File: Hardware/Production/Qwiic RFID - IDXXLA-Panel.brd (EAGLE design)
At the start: 25.4 x 30.5 mm, 60 parts, among them J2 SMD, J3 PTH, J4 SMD, J8 AVR_SPI_PROG_3X2TESTPOINTS, Q1 600mA/40V, U1 ATTINY84-ARDUINO, U2 ID-12/20SMD

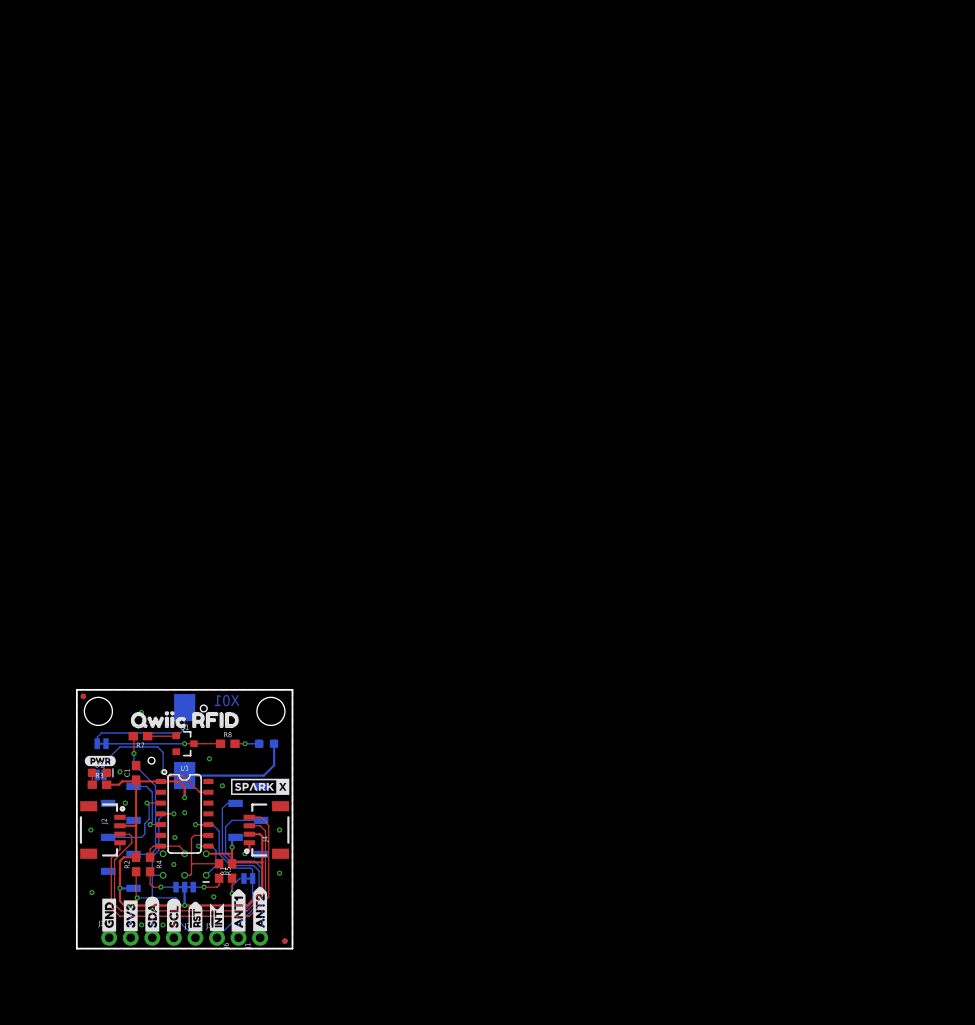
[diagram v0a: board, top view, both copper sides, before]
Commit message: Production Panel 3x3
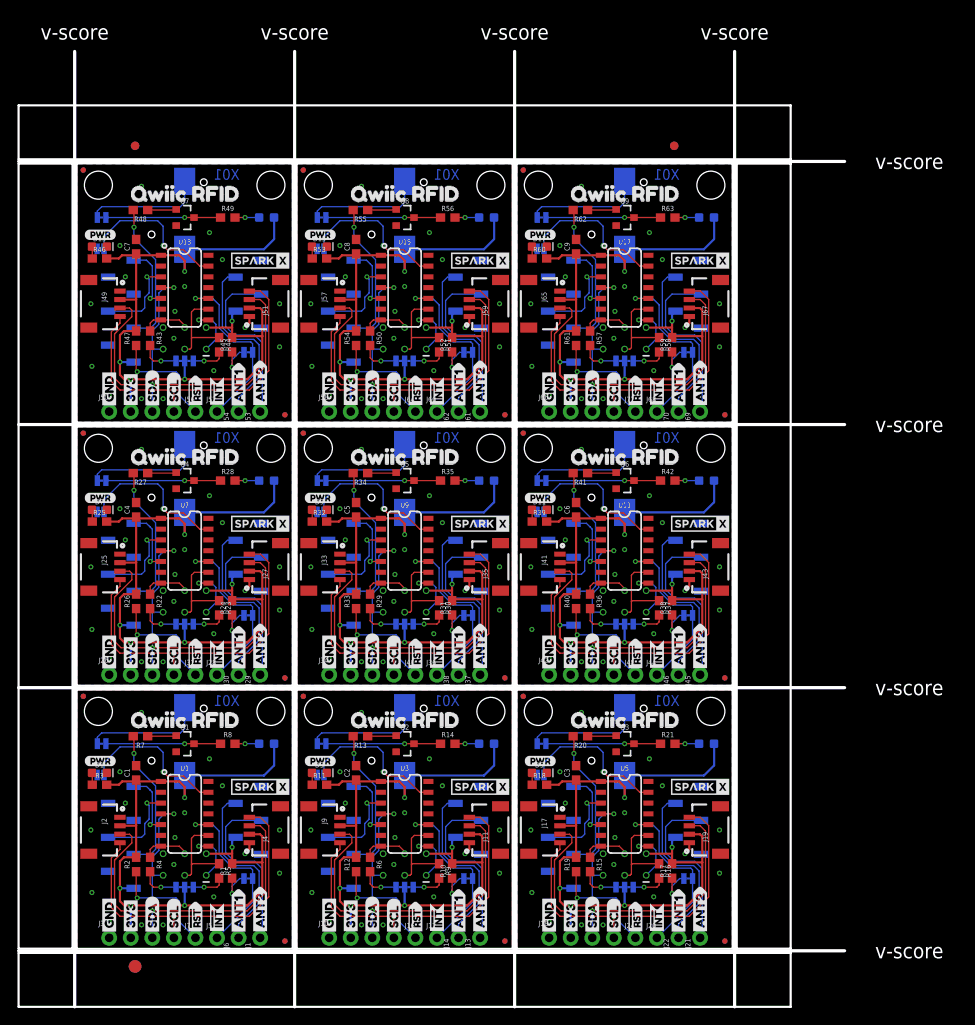
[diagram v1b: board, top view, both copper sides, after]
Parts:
- removed FRAME1: FRAME-LETTER, SparkFun-Aesthetics:CREATIVE_COMMONS
- added C2, C3, C4, C5, C6, C7, C8, C9: 0.1uF, SparkFun-Capacitors:0603
- added D10, D12, D14, D16, D18, D4, D6, D8: BLUE, SparkFun-LED:LED-0603
- added D11, D13, D15, D17, D3, D5, D7, D9: RED, SparkFun-LED:LED-0603
- added E$1, E$2, E$3, E$4: (no value), SparkFun-Aesthetics:FIDUCIAL-1X2
- added E$5, E$6: (no value), SparkFun-Retired:FIDUCIAL-1.5X3
- added I2C1, I2C2, I2C3, I2C4, I2C5, I2C6, I2C7, I2C8: (no value), SparkFun-Jumpers:SMT-JUMPER_3_2-NC_TRACE_SILK
- added J10, J18, J26, J34, J42, J50, J58, J66: PTH, SparkX:1X04_NO_SILK
- added J11, J17, J19, J25, J27, J33, J35, J41, J43, J49, J51, J57, J59, J65, J67, J9: SMD, SparkX:1X04_1MM_RA
- added J12, J13, J14, J16, J20, J21, J22, J24, J28, J29, J30, J32, J36, J37, J38, J40, J44, J45, J46, J48, J52, J53, J54, J56, J60, J61, J62, J64, J68, J69, J70, J72: (no value), SparkFun-Connectors:1X01_NO_SILK
- added J15, J23, J31, J39, J47, J55, J63, J71: AVR_SPI_PROG_3X2TESTPOINTS, SparkFun-Connectors:2X3_TEST_POINTS
- added JP10, JP11, JP19, JP20, JP28, JP29, JP37, JP38, JP46, JP47, JP55, JP56, JP64, JP65, JP73, JP74: STAND-OFF, SparkFun:STAND-OFF
- added JP12, JP13, JP14, JP15, JP21, JP22, JP23, JP24, JP30, JP31, JP32, JP33, JP39, JP40, JP41, JP42, JP48, JP49, JP50, JP51, JP57, JP58, JP59, JP60, JP66, JP67, JP68, JP69, JP75, JP76, JP77, JP78: FIDUCIALUFIDUCIAL, SparkFun:MICRO-FIDUCIAL
- added JP16, JP25, JP34, JP43, JP52, JP61, JP70, JP79: ADR, SparkFun-Jumpers:SMT-JUMPER_2_NO_SILK
- added JP17, JP26, JP35, JP44, JP53, JP62, JP71, JP80: INT, SparkFun-Jumpers:SMT-JUMPER_2_NC_TRACE_SILK
- added JP18, JP27, JP36, JP45, JP54, JP63, JP72, JP81: BUZZ, SparkFun-Jumpers:SMT-JUMPER_2_NC_TRACE_SILK
- added LOGO2, LOGO3, LOGO4, LOGO5, LOGO6, LOGO7, LOGO8, LOGO9: OSHW-LOGOMINI, SparkFun-Aesthetics:OSHW-LOGO-MINI
- added LS2, LS3, LS4, LS5, LS6, LS7, LS8, LS9: BUZZER-SMD, SparkFun-Electromechanical:BUZZER-CCV
- added Q2, Q3, Q4, Q5, Q6, Q7, Q8, Q9: 600mA/40V, SparkFun-DiscreteSemi:SOT23-3
- added R10, R12, R17, R19, R24, R26, R31, R33, R38, R40, R45, R47, R52, R54, R59, R61: 10k, SparkFun-Resistors:0603
- added R11, R13, R14, R18, R20, R21, R25, R27, R28, R32, R34, R35, R39, R41, R42, R46, R48, R49, R53, R55, R56, R60, R62, R63: 1k, SparkFun-Resistors:0603
- added R15, R16, R22, R23, R29, R30, R36, R37, R43, R44, R50, R51, R57, R58, R6, R9: 2.2k, SparkFun-Resistors:0603
- added U$100, U$126, U$152, U$178, U$204, U$230, U$48, U$74: (no value), Labels:I_SUPER2_C-()-03
- added U$101, U$127, U$153, U$179, U$205, U$231, U$49, U$75: (no value), ADR3:ADR0
- added U$102, U$128, U$154, U$180, U$206, U$232, U$50, U$76: (no value), INT3:INT0
- added U$103, U$129, U$155, U$181, U$207, U$233, U$51, U$77: (no value), Labels:PWR-()-03
- added U$104, U$130, U$156, U$182, U$208, U$234, U$52, U$78: (no value), SparkX:SPARKX-TINY
- added U$105, U$131, U$157, U$183, U$209, U$27, U$53, U$79: (no value), Labels:QWIIC-LOGO-MEDIUM
- added U$106, U$132, U$158, U$184, U$210, U$28, U$54, U$80: SPARKX-LOGO3, SparkX:SPARKX-SMALL
- added U$107, U$125, U$133, U$151, U$159, U$177, U$185, U$203, U$211, U$229, U$29, U$47, U$55, U$73, U$81, U$99: (no value), Labels:RST#-[>
- added U$108, U$122, U$134, U$148, U$160, U$174, U$186, U$200, U$212, U$226, U$30, U$44, U$56, U$70, U$82, U$96: (no value), Labels:SDA-[)
- added U$109, U$121, U$135, U$147, U$161, U$173, U$187, U$199, U$213, U$225, U$31, U$43, U$57, U$69, U$83, U$95: (no value), Labels:SCL-[)
- added U$110, U$124, U$136, U$150, U$162, U$176, U$188, U$202, U$214, U$228, U$32, U$46, U$58, U$72, U$84, U$98: (no value), Labels:GND-04
- added U$111, U$123, U$137, U$149, U$163, U$175, U$189, U$201, U$215, U$227, U$33, U$45, U$59, U$71, U$85, U$97: (no value), Labels:3V3-04
- added U$112, U$120, U$138, U$146, U$164, U$172, U$190, U$198, U$216, U$224, U$34, U$42, U$60, U$68, U$86, U$94: (no value), Labels:INT#-[<
- added U$113, U$139, U$165, U$191, U$217, U$35, U$61, U$87: (no value), BUZZER:BUZZER0
- added U$114, U$119, U$140, U$145, U$166, U$171, U$192, U$197, U$218, U$223, U$36, U$41, U$62, U$67, U$88, U$93: (no value), ANT1:ANT10
- added U$115, U$118, U$141, U$144, U$167, U$170, U$193, U$196, U$219, U$222, U$37, U$40, U$63, U$66, U$89, U$92: (no value), ANT2:ANT20
- added U$116, U$142, U$168, U$194, U$220, U$38, U$64, U$90: (no value), READ:READ0
- added U$117, U$143, U$169, U$195, U$221, U$39, U$65, U$91: (no value), QWIIC_RFID:QWIIC_RFID0
- added U10, U12, U14, U16, U18, U4, U6, U8: ID-12/20SMD, SparkFun-RF:ID-12_SMD
- added U11, U13, U15, U17, U3, U5, U7, U9: ATTINY84-ARDUINO, SparkFun-IC-Microcontroller:SO14
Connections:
- new net !INT1: J12.1, JP17.1, U3.10
- new net !INT2: J20.1, JP26.1, U5.10
- new net !INT3: J28.1, JP35.1, U7.10
- new net !INT4: J36.1, JP44.1, U9.10
- new net !INT5: J44.1, JP53.1, U11.10
- new net !INT6: J52.1, JP62.1, U13.10
- new net !INT7: J60.1, JP71.1, U15.10
- new net !INT8: J68.1, JP80.1, U17.10
- new net !RST1: J15.5, J16.1, R12.1, U3.4
- new net !RST2: J23.5, J24.1, R19.1, U5.4
- new net !RST3: J31.5, J32.1, R26.1, U7.4
- new net !RST4: J39.5, J40.1, R33.1, U9.4
- new net !RST5: J47.5, J48.1, R40.1, U11.4
- new net !RST6: J55.5, J56.1, R47.1, U13.4
- new net !RST7: J63.5, J64.1, R54.1, U15.4
- new net !RST8: J71.5, J72.1, R61.1, U17.4
- new net 3.3V1: C2.1, D4.A, I2C1.2, J10.2, J11.2, J15.2, J9.2, LS2.+, R10.2, R11.2, R12.2, U3.1, U4.11, U4.2
- new net 3.3V2: C3.1, D6.A, I2C2.2, J17.2, J18.2, J19.2, J23.2, LS3.+, R17.2, R18.2, R19.2, U5.1, U6.11, U6.2
- new net 3.3V3: C4.1, D8.A, I2C3.2, J25.2, J26.2, J27.2, J31.2, LS4.+, R24.2, R25.2, R26.2, U7.1, U8.11, U8.2
- new net 3.3V4: C5.1, D10.A, I2C4.2, J33.2, J34.2, J35.2, J39.2, LS5.+, R31.2, R32.2, R33.2, U10.11, U10.2, U9.1
- new net 3.3V5: C6.1, D12.A, I2C5.2, J41.2, J42.2, J43.2, J47.2, LS6.+, R38.2, R39.2, R40.2, U11.1, U12.11, U12.2
- new net 3.3V6: C7.1, D14.A, I2C6.2, J49.2, J50.2, J51.2, J55.2, LS7.+, R45.2, R46.2, R47.2, U13.1, U14.11, U14.2
- new net 3.3V7: C8.1, D16.A, I2C7.2, J57.2, J58.2, J59.2, J63.2, LS8.+, R52.2, R53.2, R54.2, U15.1, U16.11, U16.2
- new net 3.3V8: C9.1, D18.A, I2C8.2, J65.2, J66.2, J67.2, J71.2, LS9.+, R59.2, R60.2, R61.2, U17.1, U18.11, U18.2
- new net ANT10: J38.1, U10.4
- new net ANT11: J45.1, U12.3
- new net ANT12: J46.1, U12.4
- new net ANT13: J53.1, U14.3
- new net ANT14: J54.1, U14.4
- new net ANT15: J61.1, U16.3
- new net ANT16: J62.1, U16.4
- new net ANT17: J69.1, U18.3
- new net ANT18: J70.1, U18.4
- new net ANT3: J13.1, U4.3
- new net ANT4: J14.1, U4.4
- new net ANT5: J21.1, U6.3
- new net ANT6: J22.1, U6.4
- new net ANT7: J29.1, U8.3
- new net ANT8: J30.1, U8.4
- new net ANT9: J37.1, U10.3
- new net DATA_UART1: U3.3, U4.9
- new net DATA_UART2: U5.3, U6.9
- new net DATA_UART3: U7.3, U8.9
- new net DATA_UART4: U10.9, U9.3
- new net DATA_UART5: U11.3, U12.9
- new net DATA_UART6: U13.3, U14.9
- new net DATA_UART7: U15.3, U16.9
- new net DATA_UART8: U17.3, U18.9
- new net GND1: C2.2, D3.C, J10.1, J11.1, J15.6, J9.1, JP16.1, Q2.2, U3.14, U4.1, U4.7
- new net GND2: C3.2, D5.C, J17.1, J18.1, J19.1, J23.6, JP25.1, Q3.2, U5.14, U6.1, U6.7
- new net GND3: C4.2, D7.C, J25.1, J26.1, J27.1, J31.6, JP34.1, Q4.2, U7.14, U8.1, U8.7
- new net GND4: C5.2, D9.C, J33.1, J34.1, J35.1, J39.6, JP43.1, Q5.2, U10.1, U10.7, U9.14
- new net GND5: C6.2, D11.C, J41.1, J42.1, J43.1, J47.6, JP52.1, Q6.2, U11.14, U12.1, U12.7
- new net GND6: C7.2, D13.C, J49.1, J50.1, J51.1, J55.6, JP61.1, Q7.2, U13.14, U14.1, U14.7
- new net GND7: C8.2, D15.C, J57.1, J58.1, J59.1, J63.6, JP70.1, Q8.2, U15.14, U16.1, U16.7
- new net GND8: C9.2, D17.C, J65.1, J66.1, J67.1, J71.6, JP79.1, Q9.2, U17.14, U18.1, U18.7
- new net LED_BUZZ1: R13.2, U4.10
- new net LED_BUZZ2: R20.2, U6.10
- new net LED_BUZZ3: R27.2, U8.10
- new net LED_BUZZ4: R34.2, U10.10
- new net LED_BUZZ5: R41.2, U12.10
- new net LED_BUZZ6: R48.2, U14.10
- new net LED_BUZZ7: R55.2, U16.10
- new net LED_BUZZ8: R62.2, U18.10
- new net MISO1: J15.1, U3.8
- new net MISO2: J23.1, U5.8
- new net MISO3: J31.1, U7.8
- new net MISO4: J39.1, U9.8
- new net MISO5: J47.1, U11.8
- new net MISO6: J55.1, U13.8
- new net MISO7: J63.1, U15.8
- new net MISO8: J71.1, U17.8
- new net N$10: I2C1.1, R9.2
- new net N$11: D3.A, R11.1
- new net N$12: JP16.2, U3.13
- new net N$13: I2C1.3, R6.2
- new net N$14: JP17.2, R10.1
- new net N$15: Q2.1, R13.1
- new net N$16: JP18.1, Q2.3, R14.1
- new net N$17: D4.C, R14.2
- new net N$18: JP18.2, LS2.-
- new net N$19: I2C2.1, R16.2
- new net N$20: D5.A, R18.1
- new net N$21: JP25.2, U5.13
- new net N$22: I2C2.3, R15.2
- new net N$23: JP26.2, R17.1
- new net N$24: Q3.1, R20.1
- new net N$25: JP27.1, Q3.3, R21.1
- new net N$26: D6.C, R21.2
- new net N$27: JP27.2, LS3.-
- new net N$28: I2C3.1, R23.2
- new net N$29: D7.A, R25.1
- new net N$30: JP34.2, U7.13
- new net N$31: I2C3.3, R22.2
- new net N$32: JP35.2, R24.1
- new net N$33: Q4.1, R27.1
- new net N$34: JP36.1, Q4.3, R28.1
- new net N$35: D8.C, R28.2
- new net N$36: JP36.2, LS4.-
- new net N$37: I2C4.1, R30.2
- new net N$38: D9.A, R32.1
- new net N$39: JP43.2, U9.13
- new net N$40: I2C4.3, R29.2
- new net N$41: JP44.2, R31.1
- new net N$42: Q5.1, R34.1
- new net N$43: JP45.1, Q5.3, R35.1
- new net N$44: D10.C, R35.2
- new net N$45: JP45.2, LS5.-
- new net N$46: I2C5.1, R37.2
- new net N$47: D11.A, R39.1
- new net N$48: JP52.2, U11.13
- new net N$49: I2C5.3, R36.2
- new net N$50: JP53.2, R38.1
- new net N$51: Q6.1, R41.1
- new net N$52: JP54.1, Q6.3, R42.1
- new net N$53: D12.C, R42.2
- new net N$54: JP54.2, LS6.-
- new net N$55: I2C6.1, R44.2
- new net N$56: D13.A, R46.1
- new net N$57: JP61.2, U13.13
- new net N$58: I2C6.3, R43.2
- new net N$59: JP62.2, R45.1
- new net N$60: Q7.1, R48.1
- new net N$61: JP63.1, Q7.3, R49.1
- new net N$62: D14.C, R49.2
- new net N$63: JP63.2, LS7.-
- new net N$64: I2C7.1, R51.2
- new net N$65: D15.A, R53.1
- new net N$66: JP70.2, U15.13
- new net N$67: I2C7.3, R50.2
- new net N$68: JP71.2, R52.1
- new net N$69: Q8.1, R55.1
- new net N$70: JP72.1, Q8.3, R56.1
- new net N$71: D16.C, R56.2
- new net N$72: JP72.2, LS8.-
- new net N$73: I2C8.1, R58.2
- new net N$74: D17.A, R60.1
- new net N$75: JP79.2, U17.13
- new net N$76: I2C8.3, R57.2
- new net N$77: JP80.2, R59.1
- new net N$78: Q9.1, R62.1
- new net N$79: JP81.1, Q9.3, R63.1
- new net N$80: D18.C, R63.2
- new net N$81: JP81.2, LS9.-
- new net SCL/SCK1: J15.3, R9.1, U3.9
- new net SCL/SCK2: J23.3, R16.1, U5.9
- new net SCL/SCK3: J31.3, R23.1, U7.9
- new net SCL/SCK4: J39.3, R30.1, U9.9
- new net SCL/SCK5: J47.3, R37.1, U11.9
- new net SCL/SCK6: J55.3, R44.1, U13.9
- new net SCL/SCK7: J63.3, R51.1, U15.9
- new net SCL/SCK8: J71.3, R58.1, U17.9
- new net SCL1: J10.4, J11.4, J9.4
- new net SCL2: J17.4, J18.4, J19.4
- new net SCL3: J25.4, J26.4, J27.4
- new net SCL4: J33.4, J34.4, J35.4
- new net SCL5: J41.4, J42.4, J43.4
- new net SCL6: J49.4, J50.4, J51.4
- new net SCL7: J57.4, J58.4, J59.4
- new net SCL8: J65.4, J66.4, J67.4
- new net SDA/MOSI1: J15.4, R6.1, U3.7
- new net SDA/MOSI2: J23.4, R15.1, U5.7
- new net SDA/MOSI3: J31.4, R22.1, U7.7
- new net SDA/MOSI4: J39.4, R29.1, U9.7
- new net SDA/MOSI5: J47.4, R36.1, U11.7
- new net SDA/MOSI6: J55.4, R43.1, U13.7
- new net SDA/MOSI7: J63.4, R50.1, U15.7
- new net SDA/MOSI8: J71.4, R57.1, U17.7
- new net SDA1: J10.3, J11.3, J9.3
- new net SDA2: J17.3, J18.3, J19.3
- new net SDA3: J25.3, J26.3, J27.3
- new net SDA4: J33.3, J34.3, J35.3
- new net SDA5: J41.3, J42.3, J43.3
- new net SDA6: J49.3, J50.3, J51.3
- new net SDA7: J57.3, J58.3, J59.3
- new net SDA8: J65.3, J66.3, J67.3
- new net TAG_IN_RANGE1: U3.5, U4.6
- new net TAG_IN_RANGE2: U5.5, U6.6
- new net TAG_IN_RANGE3: U7.5, U8.6
- new net TAG_IN_RANGE4: U10.6, U9.5
- new net TAG_IN_RANGE5: U11.5, U12.6
- new net TAG_IN_RANGE6: U13.5, U14.6
- new net TAG_IN_RANGE7: U15.5, U16.6
- new net TAG_IN_RANGE8: U17.5, U18.6
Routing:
- net 3.3V4: track 0.00 -> 88.3 mm, vias 0 -> 5
- net 3.3V3: track 0.00 -> 88.3 mm, vias 0 -> 5
- net 3.3V1: track 0.00 -> 88.3 mm, vias 0 -> 5
- net 3.3V5: track 0.00 -> 88.3 mm, vias 0 -> 5
- net 3.3V7: track 0.00 -> 88.3 mm, vias 0 -> 5
- net 3.3V6: track 0.00 -> 88.3 mm, vias 0 -> 5
- net 3.3V2: track 0.00 -> 88.3 mm, vias 0 -> 5
- net 3.3V8: track 0.00 -> 88.3 mm, vias 0 -> 5
- net SDA2: track 0.00 -> 42.4 mm, vias 0 -> 1
- net SDA1: track 0.00 -> 42.4 mm, vias 0 -> 1
- net SDA7: track 0.00 -> 42.4 mm, vias 0 -> 1
- net SDA3: track 0.00 -> 42.4 mm, vias 0 -> 1
- net SDA8: track 0.00 -> 42.4 mm, vias 0 -> 1
- net SDA6: track 0.00 -> 42.4 mm, vias 0 -> 1
- net SDA5: track 0.00 -> 42.4 mm, vias 0 -> 1
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- added copper zone on layer 1, net GND1
- added copper zone on layer 16, net GND1
- added copper zone on layer 1, net GND2
- added copper zone on layer 16, net GND2
- added copper zone on layer 1, net GND3
- added copper zone on layer 16, net GND3
- added copper zone on layer 1, net GND4
- added copper zone on layer 16, net GND4
- added copper zone on layer 1, net GND5
- added copper zone on layer 16, net GND5
- added copper zone on layer 1, net GND6
- added copper zone on layer 16, net GND6
- added copper zone on layer 1, net GND7
- added copper zone on layer 16, net GND7
- added copper zone on layer 1, net GND8
- added copper zone on layer 16, net GND8
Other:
- board size 25.4 x 30.5 mm -> 97.3 x 112.5 mm
- board text added: "v-score"
- board text removed: "Elias Santistevan"
- board text removed: "Units in Inches"

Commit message: Panel for x02
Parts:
- moved U$100 0.38 mm to (14.1, 40.9)
- moved U$126 0.38 mm to (40.0, 40.9)
- moved U$152 0.38 mm to (65.9, 40.9)
- moved U$178 0.38 mm to (14.1, 71.9)
- moved U$2 0.38 mm to (14.1, 9.91)
- moved U$204 0.38 mm to (40.0, 71.9)
- moved U$230 0.38 mm to (65.9, 71.9)
- moved U$48 0.38 mm to (40.0, 9.91)
- moved U$74 0.38 mm to (65.9, 9.91)
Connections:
- removed net SCL: J2.4, J3.4, J4.4
- removed net SCL1: J10.4, J11.4, J9.4
- removed net SCL2: J17.4, J18.4, J19.4
- removed net SCL3: J25.4, J26.4, J27.4
- removed net SCL4: J33.4, J34.4, J35.4
- removed net SCL5: J41.4, J42.4, J43.4
- removed net SCL6: J49.4, J50.4, J51.4
- removed net SCL7: J57.4, J58.4, J59.4
- removed net SCL8: J65.4, J66.4, J67.4
- removed net SDA: J2.3, J3.3, J4.3
- removed net SDA1: J10.3, J11.3, J9.3
- removed net SDA2: J17.3, J18.3, J19.3
- removed net SDA3: J25.3, J26.3, J27.3
- removed net SDA4: J33.3, J34.3, J35.3
- removed net SDA5: J41.3, J42.3, J43.3
- removed net SDA6: J49.3, J50.3, J51.3
- removed net SDA7: J57.3, J58.3, J59.3
- removed net SDA8: J65.3, J66.3, J67.3
- net DATA_UART: now also U1.11; no longer U1.3
- net DATA_UART1: now also U3.11; no longer U3.3
- net DATA_UART2: now also U5.11; no longer U5.3
- net DATA_UART3: now also U7.11; no longer U7.3
- net DATA_UART4: now also U9.11; no longer U9.3
- net DATA_UART5: now also U11.11; no longer U11.3
- net DATA_UART6: now also U13.11; no longer U13.3
- net DATA_UART7: now also U15.11; no longer U15.3
- net DATA_UART8: now also U17.11; no longer U17.3
- net SCL/SCK: now also J2.4, J3.4, J4.4
- net SCL/SCK1: now also J10.4, J11.4, J9.4
- net SCL/SCK2: now also J17.4, J18.4, J19.4
- net SCL/SCK3: now also J25.4, J26.4, J27.4
- net SCL/SCK4: now also J33.4, J34.4, J35.4
- net SCL/SCK5: now also J41.4, J42.4, J43.4
- net SCL/SCK6: now also J49.4, J50.4, J51.4
- net SCL/SCK7: now also J57.4, J58.4, J59.4
- net SCL/SCK8: now also J65.4, J66.4, J67.4
- net SDA/MOSI: now also J2.3, J3.3, J4.3
- net SDA/MOSI1: now also J10.3, J11.3, J9.3
- net SDA/MOSI2: now also J17.3, J18.3, J19.3
- net SDA/MOSI3: now also J25.3, J26.3, J27.3
- net SDA/MOSI4: now also J33.3, J34.3, J35.3
- net SDA/MOSI5: now also J41.3, J42.3, J43.3
- net SDA/MOSI6: now also J49.3, J50.3, J51.3
- net SDA/MOSI7: now also J57.3, J58.3, J59.3
- net SDA/MOSI8: now also J65.3, J66.3, J67.3
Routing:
- net SCL/SCK4: track 10.5 -> 57.4 mm, vias 0 -> 3
- net SCL/SCK7: track 10.5 -> 57.4 mm, vias 0 -> 3
- net SCL/SCK6: track 10.5 -> 57.4 mm, vias 0 -> 3
- net SCL/SCK: track 10.5 -> 57.4 mm, vias 0 -> 3
- net SCL/SCK5: track 10.5 -> 57.4 mm, vias 0 -> 3
- net SCL/SCK1: track 10.5 -> 57.4 mm, vias 0 -> 3
- net SCL/SCK8: track 10.5 -> 57.4 mm, vias 0 -> 3
- net SCL/SCK3: track 10.5 -> 57.4 mm, vias 0 -> 3
- net SCL/SCK2: track 10.5 -> 57.4 mm, vias 0 -> 3
- net SDA/MOSI2: track 5.67 -> 50.6 mm, vias 0 -> 3
- net SDA/MOSI: track 5.67 -> 50.6 mm, vias 0 -> 3
- net SDA/MOSI7: track 5.67 -> 50.6 mm, vias 0 -> 3
- net SDA/MOSI4: track 5.67 -> 50.6 mm, vias 0 -> 3
- net SDA/MOSI1: track 5.67 -> 50.6 mm, vias 0 -> 3
- net SDA/MOSI6: track 5.67 -> 50.6 mm, vias 0 -> 3
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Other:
- board text added: "X02"
- board text removed: "X01"

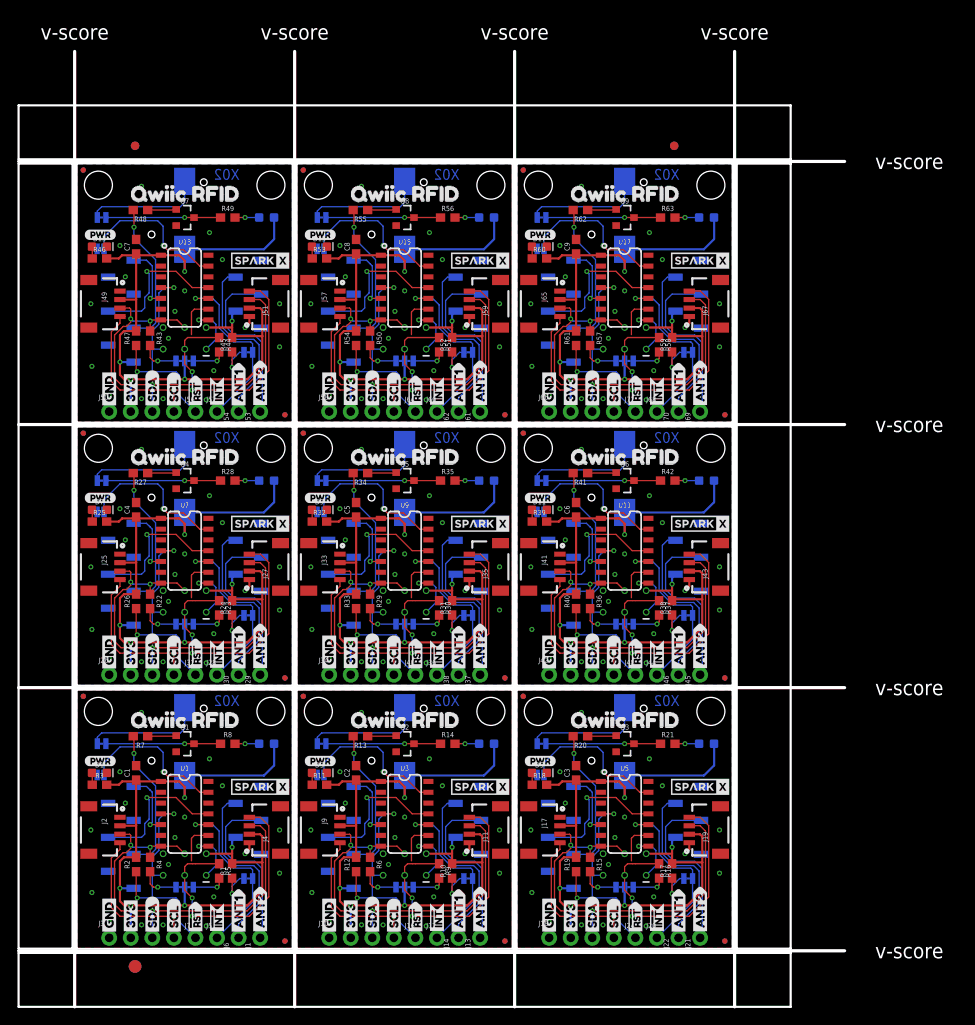
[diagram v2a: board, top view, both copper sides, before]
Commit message: Fixed DRC erros added latest panel for x02
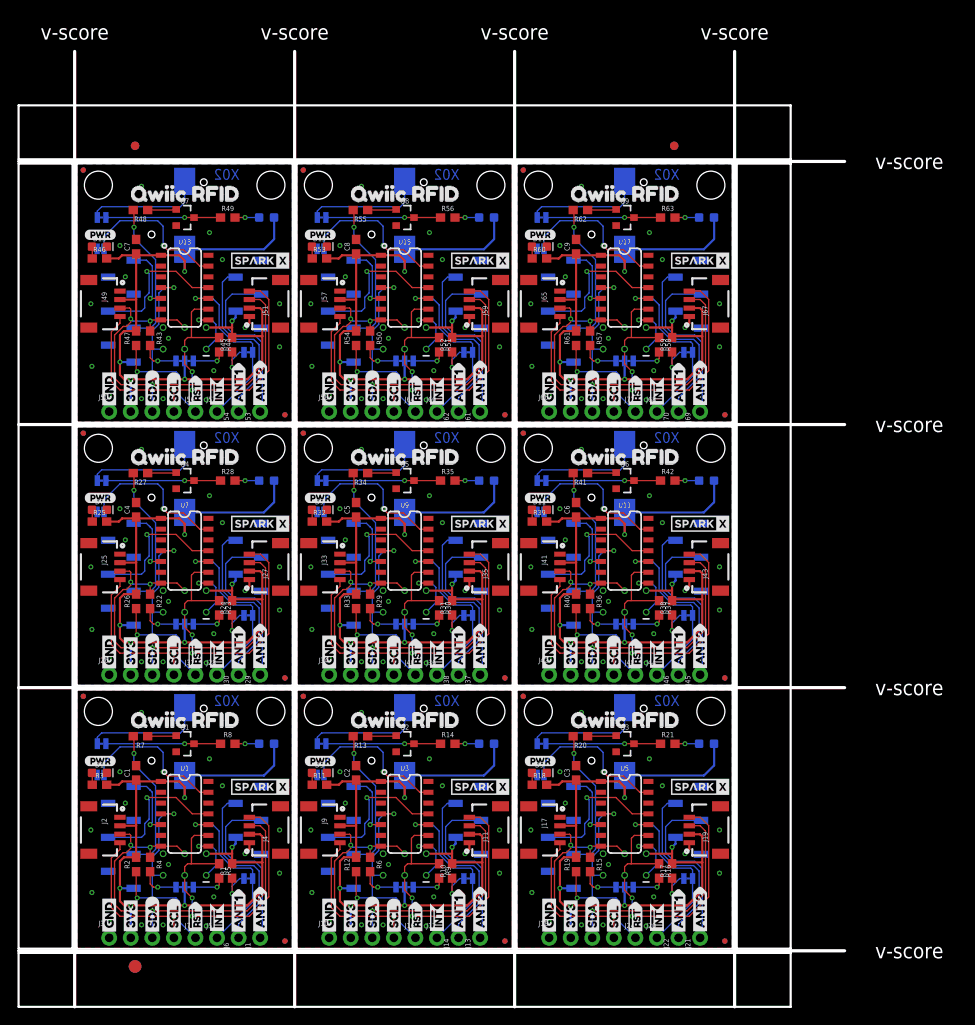
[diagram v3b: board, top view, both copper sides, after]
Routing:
- net SDA/MOSI4: track 50.6 -> 50.1 mm
- net SDA/MOSI3: track 50.6 -> 50.1 mm
- net SDA/MOSI2: track 50.6 -> 50.1 mm
- net SDA/MOSI8: track 50.6 -> 50.1 mm
- net SDA/MOSI7: track 50.6 -> 50.1 mm
- net SDA/MOSI6: track 50.6 -> 50.1 mm
- net SDA/MOSI5: track 50.6 -> 50.1 mm
- net SDA/MOSI1: track 50.6 -> 50.1 mm
- net SDA/MOSI: track 50.6 -> 50.1 mm
- net GND8: vias 18 -> 16
- net GND7: vias 18 -> 16
- net GND6: vias 18 -> 16
- net GND5: vias 18 -> 16
- net GND4: vias 18 -> 16
- net GND3: vias 18 -> 16
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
